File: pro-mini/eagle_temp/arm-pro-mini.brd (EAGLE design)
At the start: 38.1 x 20.3 mm, 61 parts, among them J1 MICRO USB, J2 SWD HEADER, Q1 12Mhz, T1 MMBT3906, U1 PRTR5V0U2X, U2 MIC5225-3.3v, U3 LPC11U35FHI33/501, U4 BAS40-05

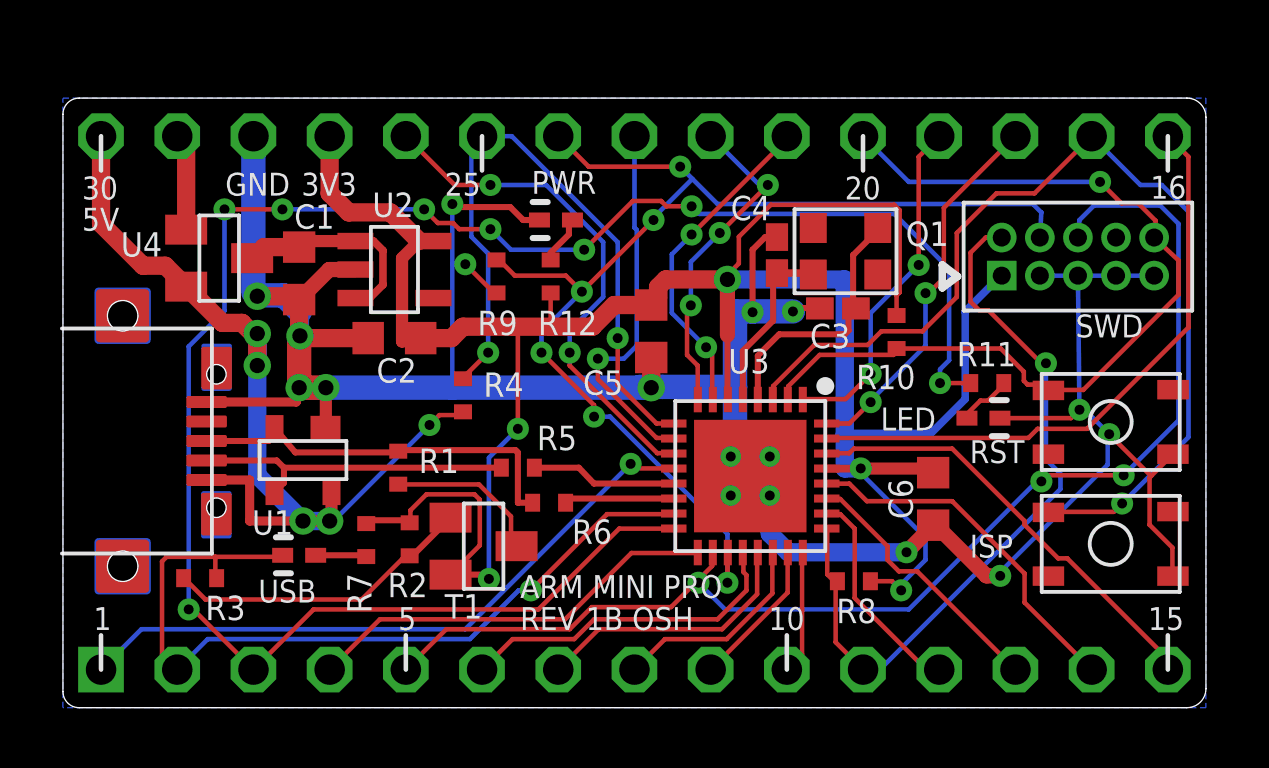
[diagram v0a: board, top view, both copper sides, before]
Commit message: Work in progress. Layout auto routs 100%. Requires net list and footprints verification.
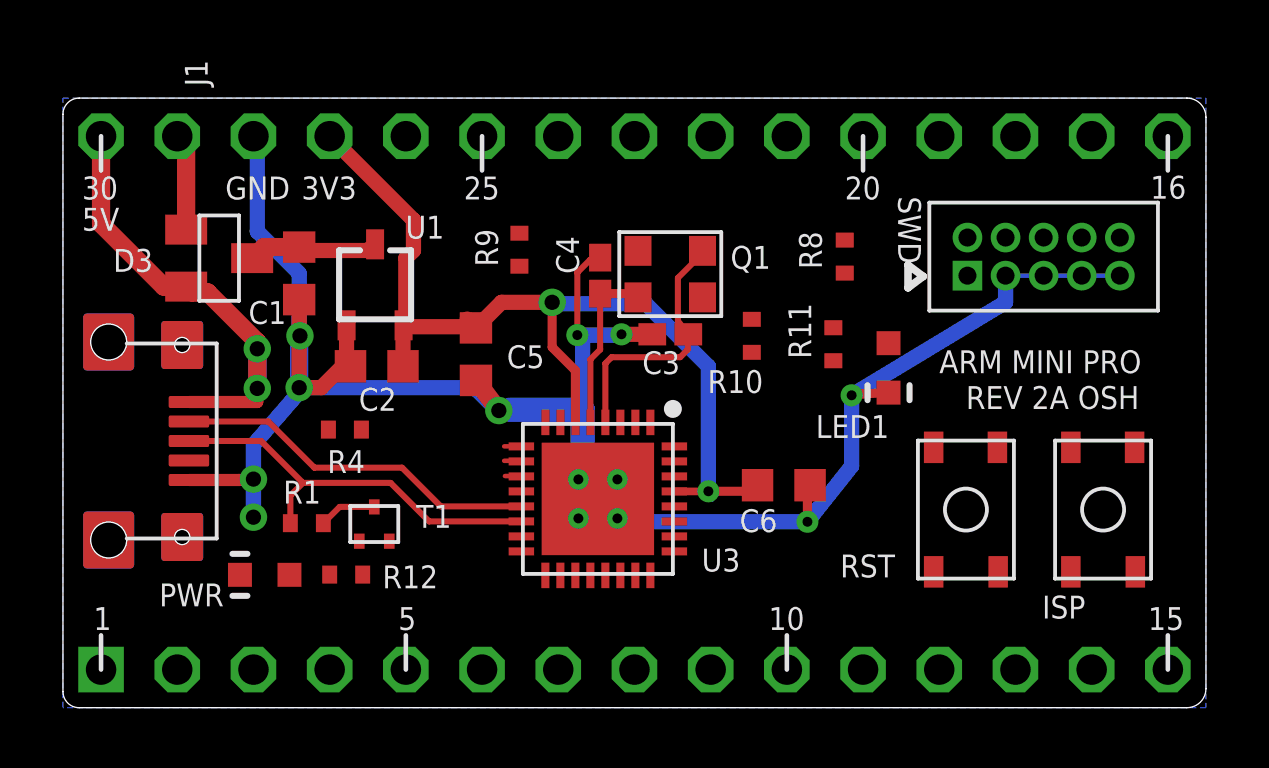
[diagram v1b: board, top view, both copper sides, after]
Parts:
- removed LED1: Green, arm-pro-mini:CHIP-LED0603
- removed LED2: Red, arm-pro-mini:CHIP-LED0603
- removed LED3: Blue, arm-pro-mini:CHIP-LED0603
- removed R2: 10K, arm-pro-mini:R0402
- removed R3, R7: 1K5, arm-pro-mini:R0402
- removed R5, R6: 33R, arm-pro-mini:R0402
- removed U2: MIC5225-3.3v, arm-pro-mini:SOT25
- added D1: RED, arm-pro-mini:LED0603
- added D2: GRN, arm-pro-mini:LED0603
- C1, C2: value 2u2 -> 1u
- J1: value MICRO USB -> USB; device arm-pro-mini:USB-MICRO-ZX62RD-AB-5P8 -> arm-pro-mini:USB-MICRO
- T1: value MMBT3906 -> DTA114EET1G (2 X 10K); device arm-pro-mini:SOT23-BEC -> arm-pro-mini:SC75-BEC
- U1: value PRTR5V0U2X -> MCP1754ST-3302E/CB; device arm-pro-mini:SOT143B -> arm-pro-mini:SOT-23A
- moved R12 12.1 mm to (9.44, 4.44), turned to 0 degrees
- moved R8 10.8 mm to (26.1, 15.0), turned to 270 degrees
- moved U1 6.32 mm to (10.4, 14.1), turned to 0 degrees
- moved C4 5.93 mm to (17.9, 14.4)
- moved C5 5.89 mm to (13.8, 11.8)
- moved Q1 5.89 mm to (20.2, 14.5)
- moved C3 5.65 mm to (20.2, 12.4)
- moved S2 5.64 mm to (30.1, 6.60), turned to 90 degrees
- moved R11 5.29 mm to (25.7, 12.1), turned to 90 degrees
- moved U3 5.14 mm to (17.8, 6.96)
- moved C6 5.00 mm to (24.0, 7.42), turned to 0 degrees
- moved R10 4.83 mm to (23.0, 12.4)
- moved R4 4.10 mm to (9.40, 9.27), turned to 0 degrees
- moved T1 3.72 mm to (10.4, 6.12), turned to 0 degrees
- moved R1 3.56 mm to (8.13, 6.15), turned to 0 degrees
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- renumbered U4 to D3
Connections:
- removed net N$4: R2.1, R3.1, T1.B
- removed net N$7: LED1.A, R7.1
- removed net N$8: J1.3, R1.1, R6.1, U1.2
- removed net N$9: J1.2, R5.1, U1.3
- removed net PIO0_20: TP21.1, U3.7
- removed net PIO0_7-LED: R11.2, TP3.1, U3.16
- new net PIO0_20-LED1: R11.2, TP21.1, U3.7
- new net PIO0_7: TP3.1, U3.16
- net +3V3: now also U1.VOUT; no longer R2.2, R7.2, U2.5
- net GND: now also D1.C, D2.C, U1.GND; no longer LED2.C, LED3.C, U1.1, U2.2
- net N$10: now also U1.VIN; no longer U2.1, U2.3
- net N$2: now also D2.A; no longer LED3.A
- net N$6: now also D1.A; no longer LED2.A
- net PIO0_6-CONNECT: now also T1.B; no longer LED1.C, R3.2
- net USB-5V: no longer U1.4
- net USB_DM: now also J1.2; no longer R5.2
- net USB_DP: now also J1.3, R1.1; no longer R6.2
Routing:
- net PIO0_7-LED: track 64.1 -> 0.00 mm, vias 8 -> 0
- net +3V3: track 85.4 -> 32.8 mm, vias 5 -> 2
- net PIO0_9-SWDO: track 42.0 -> 0.00 mm, vias 3 -> 0
- net PIO0_10-SWDCLK: track 40.8 -> 0.00 mm, vias 6 -> 0
- net PIO0_1-ISP_EN: track 33.4 -> 0.15 mm, vias 1 -> 0
- net GND: track 106.5 -> 75.7 mm, vias 13 -> 9
- net PIO0_0-RESET: track 30.0 -> 0.03 mm, vias 1 -> 0
- net PIO0_6-CONNECT: track 27.5 -> 0.00 mm, vias 1 -> 0
- net PIO0_15-SWDIO: track 25.4 -> 0.02 mm, vias 1 -> 0
- net PIO0_21: track 22.0 -> 0.00 mm, vias 1 -> 0
- net PIO0_3-VBUS: track 22.0 -> 0.57 mm, vias 2 -> 0
- net PIO0_18: track 20.2 -> 0.00 mm
- net PIO0_5: track 17.3 -> 0.55 mm, vias 2 -> 0
- net USB-5V: track 32.0 -> 16.7 mm, vias 5 -> 2
- net PIO0_17: track 14.8 -> 0.02 mm
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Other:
- board text added: "LED1"
- board text added: "REV 2A OSH"
- board text removed: "LED"
- board text removed: "REV 1B OSH"
- board text removed: "USB"

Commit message: Ready for final auto routing.
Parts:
- removed R8: 10K, arm-pro-mini:R0402
- added R2: 10K, arm-pro-mini:R0402
- TP1: device arm-pro-mini:1X01-SQUARE -> arm-pro-mini:1X01
- moved R4 17.6 mm to (26.1, 15.0), turned to 270 degrees
- renumbered R10 to R5, R11 to R7, R12 to R6, R9 to R3
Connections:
- net +3V3: now also R4.2; no longer R8.2
- net GND: now also J1.G1, J1.G2, J1.G3, J1.G4
- net PIO0_15-SWDIO: now also R4.1; no longer R8.1
- net PIO0_3-VBUS: now also R2.2; no longer R4.2
- net USB-5V: now also R2.1; no longer R4.1
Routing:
- net GND: track 75.7 -> 89.5 mm
- net +3V3: track 32.8 -> 34.0 mm

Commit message: Tweaked the layout. Ready for final auto routing.
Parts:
- moved R6 1.80 mm to (8.17, 5.71)
- moved R1 0.63 mm to (8.13, 6.79)
- moved D2 0.52 mm to (7.23, 4.56)
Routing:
- net GND: track 89.5 -> 93.1 mm
- net USB-5V: track 16.7 -> 14.0 mm, vias 2 -> 0
- net N$5: track 1.92 -> 0.00 mm
- net USB_DP: track 13.7 -> 12.2 mm
- net PIO0_4: track 0.58 -> 0.03 mm
- net PIO0_3-VBUS: track 0.57 -> 0.02 mm
- net PIO0_5: track 0.55 -> 0.02 mm

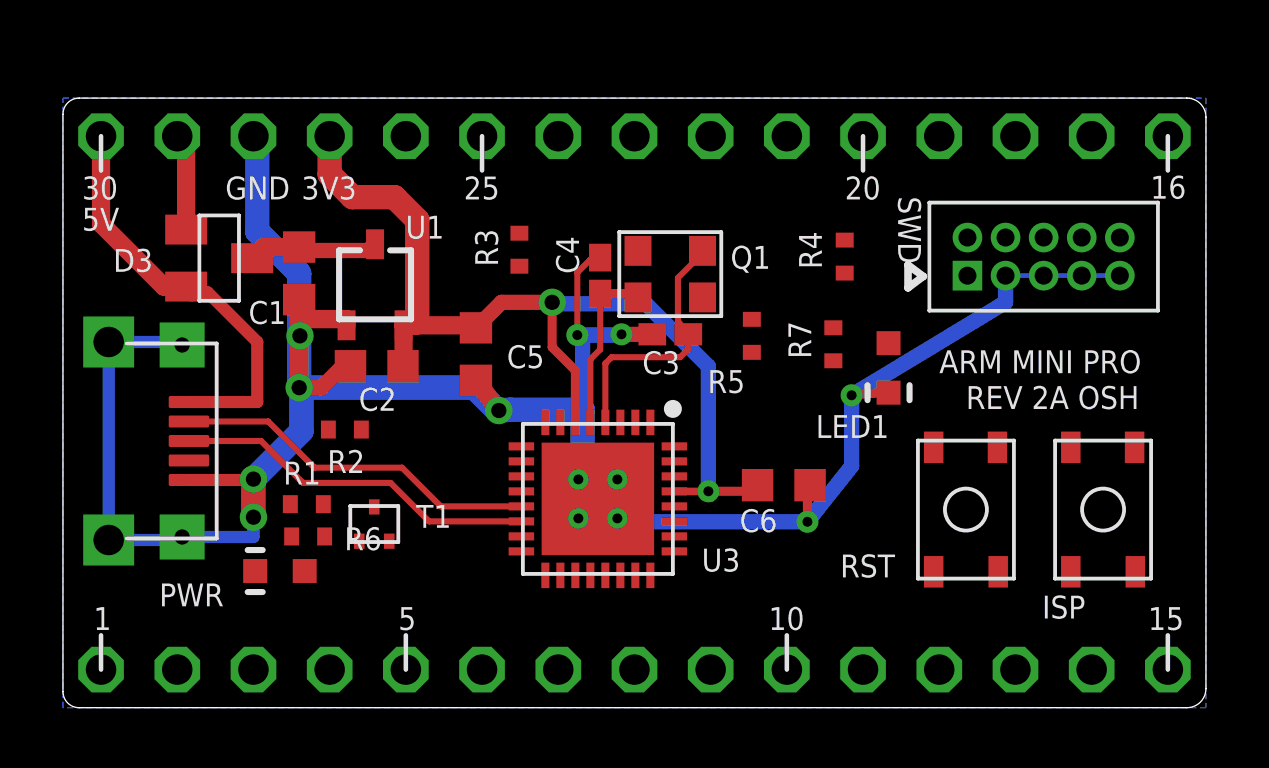
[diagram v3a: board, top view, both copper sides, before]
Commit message: Perform final auto routing.
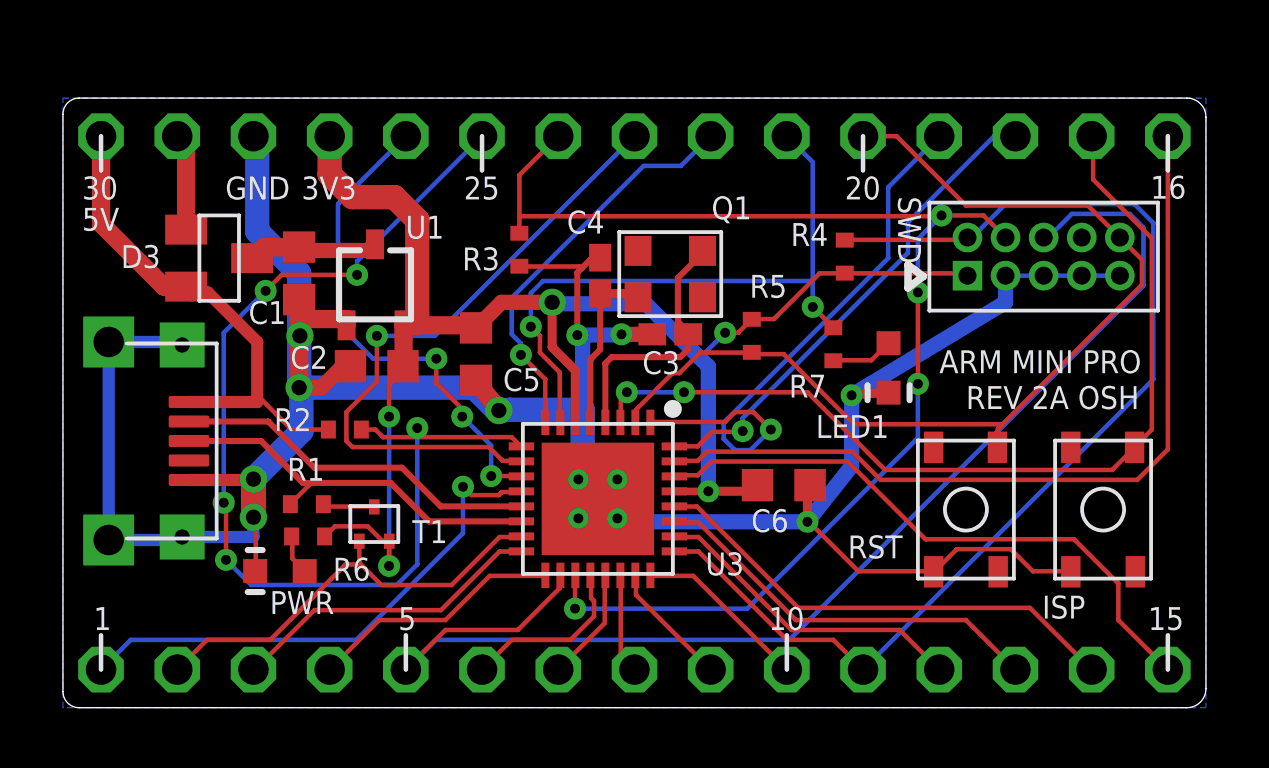
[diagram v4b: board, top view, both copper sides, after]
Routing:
- net PIO0_10-SWDCLK: track 0.00 -> 42.9 mm, vias 0 -> 4
- net PIO0_9-SWDO: track 0.00 -> 42.4 mm
- net PIO0_15-SWDIO: track 0.02 -> 37.9 mm
- net PIO0_3-VBUS: track 0.02 -> 36.6 mm, vias 0 -> 5
- net PIO0_0-RESET: track 0.03 -> 33.7 mm
- net PIO0_1-ISP_EN: track 0.15 -> 31.0 mm, vias 0 -> 2
- net PIO0_18: track 0.00 -> 27.8 mm
- net PIO0_4: track 0.03 -> 21.4 mm, vias 0 -> 1
- net PIO0_20-LED1: track 0.00 -> 21.3 mm, vias 0 -> 2
- net +3V3: track 34.0 -> 54.3 mm, vias 2 -> 5
- net PIO0_17: track 0.02 -> 20.3 mm
- net PIO1_19: track 0.00 -> 19.5 mm, vias 0 -> 1
- net PIO0_21: track 0.00 -> 17.6 mm, vias 0 -> 1
- net PIO0_5: track 0.02 -> 16.6 mm, vias 0 -> 3
- net PIO0_19: track 0.00 -> 16.5 mm, vias 0 -> 1
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
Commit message: Added esd protection
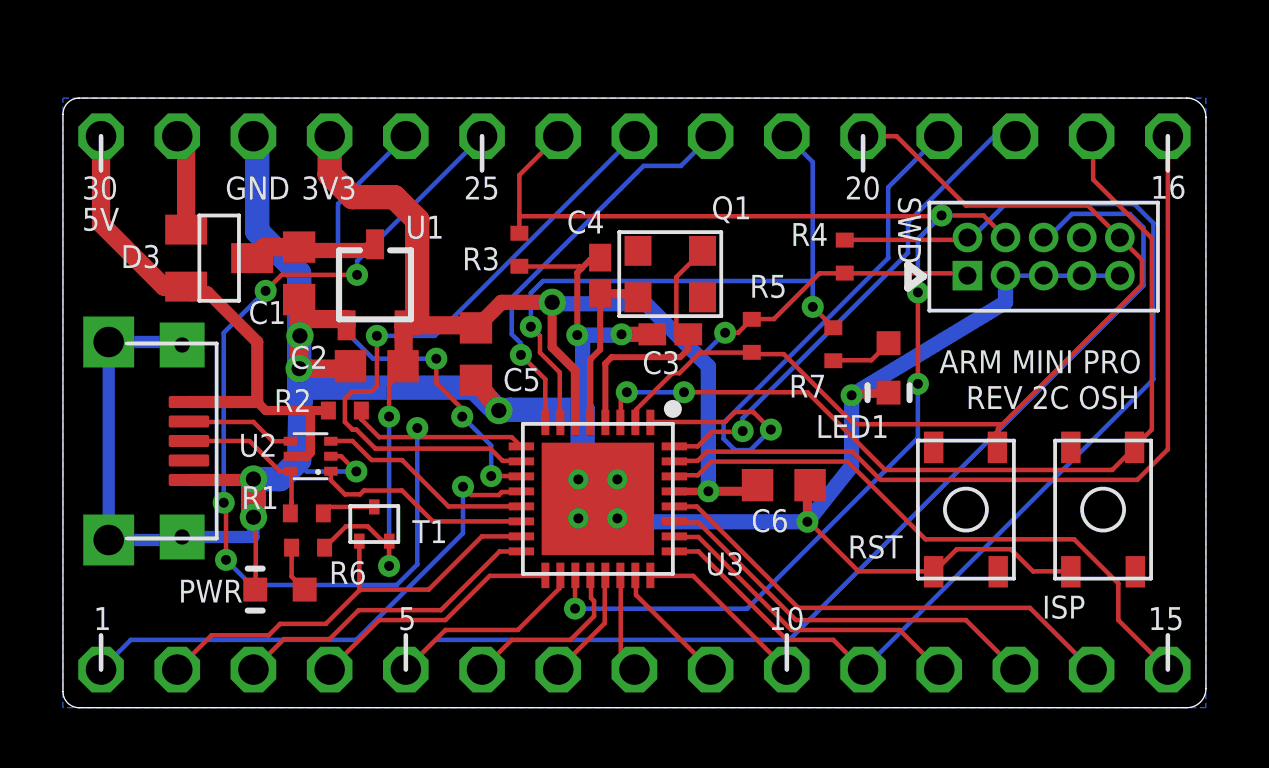
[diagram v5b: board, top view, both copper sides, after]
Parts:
- added U2: NUF2042XV6T1G, arm-pro-mini:SOT-563
- moved R2 0.63 mm to (9.40, 9.91)
- moved D2 0.62 mm to (7.23, 3.94)
- moved R6 0.37 mm to (8.17, 5.33)
- moved R1 0.31 mm to (8.13, 6.48)
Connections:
- new net N$4: J1.2, U2.4
- new net N$7: J1.3, R1.1, U2.6
- net GND: now also U2.2
- net USB-5V: now also U2.5
- net USB_DM: now also U2.3; no longer J1.2
- net USB_DP: now also U2.1; no longer J1.3, R1.1
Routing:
- net USB_DP: track 13.2 -> 7.34 mm
- net GND: track 107.0 -> 112.4 mm, vias 9 -> 10
- net N$7: track 0.00 -> 5.24 mm
- net USB_DM: track 12.3 -> 7.26 mm
- net N$4: track 0.00 -> 3.65 mm
- net USB-5V: track 16.8 -> 18.7 mm
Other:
- board text added: "REV 2C OSH"
- board text removed: "REV 2A OSH"

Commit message: Updated arm-pro-mini (new/temp)
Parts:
- R1: value 1k5 -> 1K5
- R6: value 10K -> 1K5
- moved S2 1.00 mm to (31.1, 6.60)
- moved R6 0.61 mm to (7.62, 5.08)
- moved D2 0.25 mm to (7.23, 3.68)
- moved R1 0.13 mm to (8.13, 6.60)
- moved T1 0.08 mm to (10.4, 6.05)
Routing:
- net +3V3: track 54.4 -> 55.2 mm
- net PIO0_18: track 27.8 -> 28.6 mm
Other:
- board text added: "REV 2D OSH"
- board text removed: "REV 2C OSH"
